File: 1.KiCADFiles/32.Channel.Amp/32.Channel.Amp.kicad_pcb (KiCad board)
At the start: 2 copper layers, 64 x 3 mm, 1 part

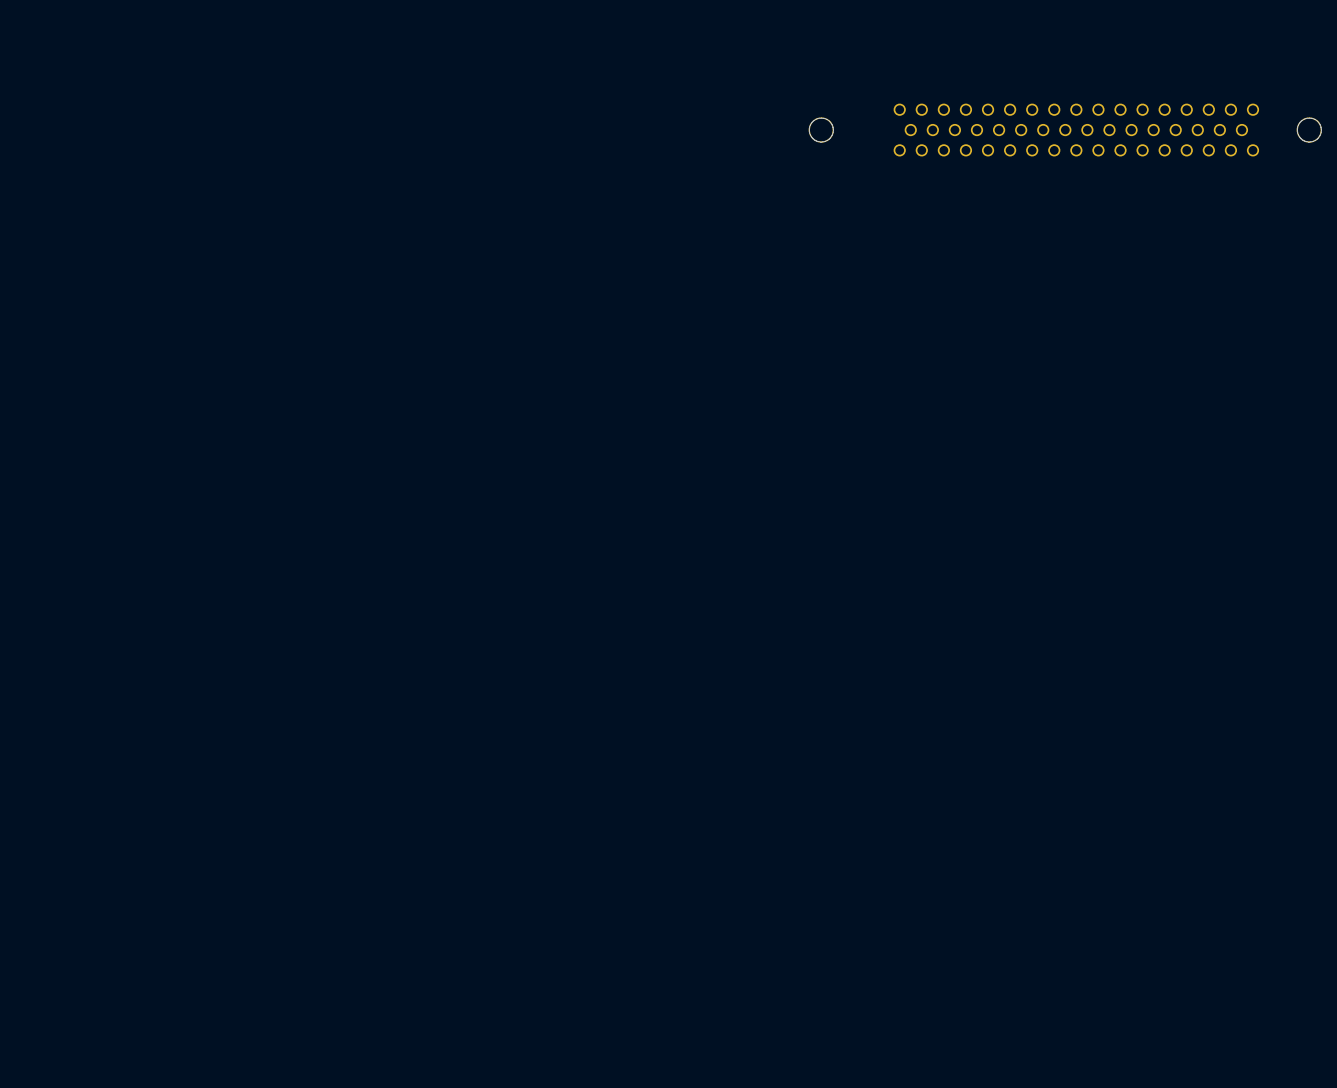
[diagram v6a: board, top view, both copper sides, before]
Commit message: Template Format Created for 32 Channel Amp
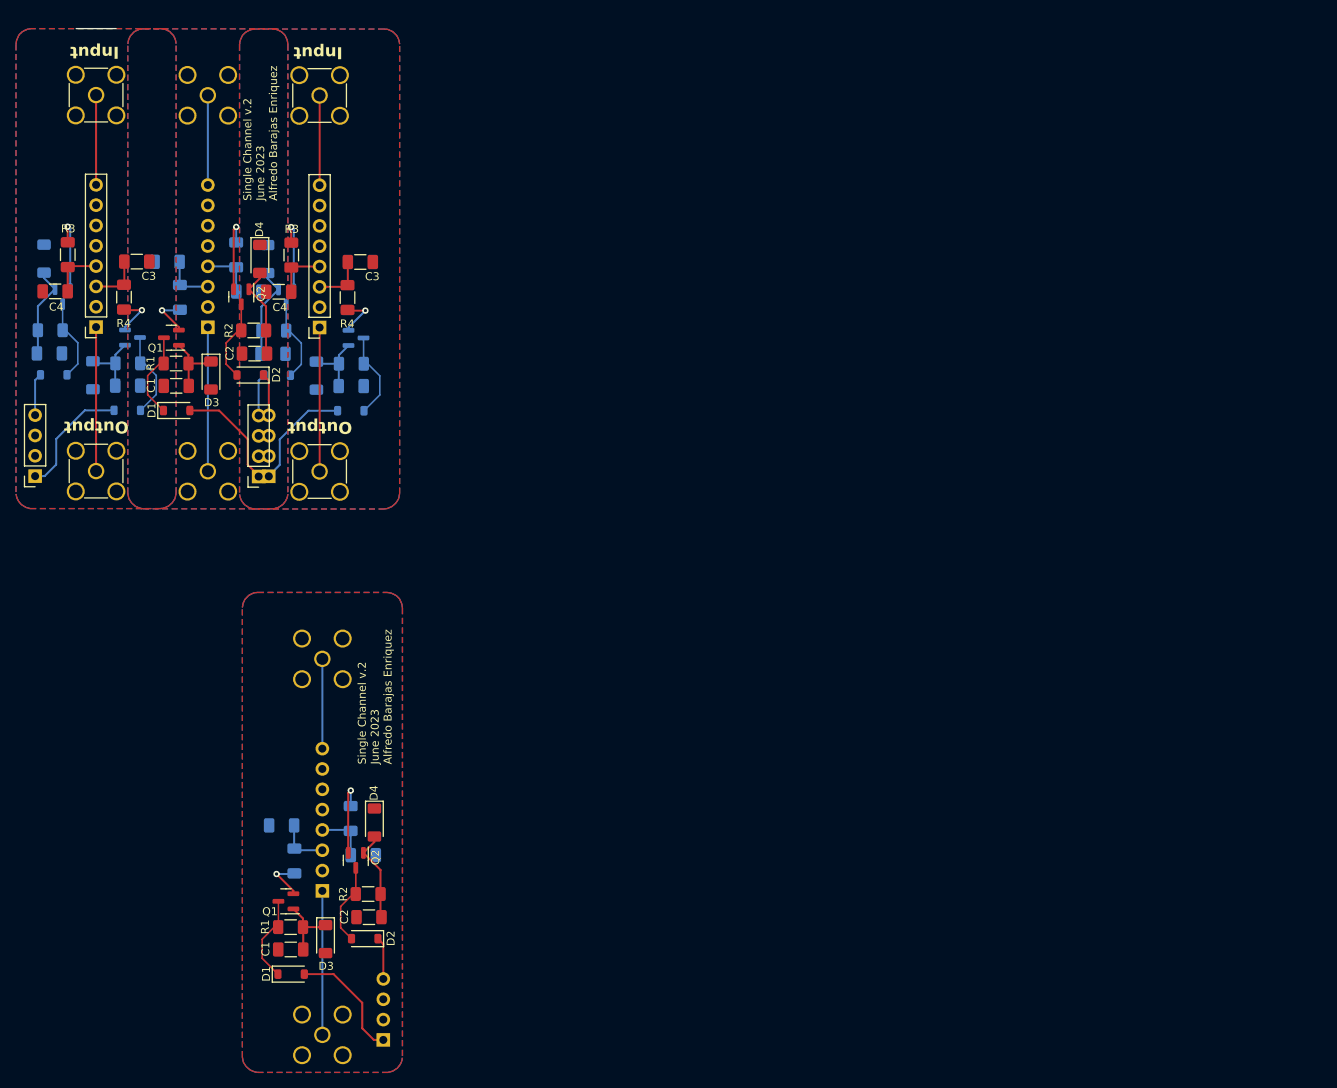
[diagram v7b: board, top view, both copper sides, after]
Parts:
- removed REF**: CONN D-SUB PLUG 50POS RA SLDR, 1.Local.Library:CONN D-SUB PLUG 50POS RA SLDR
- added C1: 10uF, Capacitor_SMD:C_1206_3216Metric_Pad1.33x1.80mm_HandSolder, F.Cu at (31.5, 59.4)
- added C1: 10uF, Capacitor_SMD:C_1206_3216Metric_Pad1.33x1.80mm_HandSolder, F.Cu at (45.8, 129.9)
- added C1: 10uF, Capacitor_SMD:C_1206_3216Metric_Pad1.33x1.80mm_HandSolder, B.Cu at (53.4, 59.5)
- added C1: 10uF, Capacitor_SMD:C_1206_3216Metric_Pad1.33x1.80mm_HandSolder, B.Cu at (25.4, 59.4)
- added C2: 10uF, Capacitor_SMD:C_1206_3216Metric_Pad1.33x1.80mm_HandSolder, F.Cu at (41.3, 55.4)
- added C2: 10uF, Capacitor_SMD:C_1206_3216Metric_Pad1.33x1.80mm_HandSolder, F.Cu at (55.6, 125.9)
- added C2: 10uF, Capacitor_SMD:C_1206_3216Metric_Pad1.33x1.80mm_HandSolder, B.Cu at (15.6, 55.4)
- added C2: 10uF, Capacitor_SMD:C_1206_3216Metric_Pad1.33x1.80mm_HandSolder, B.Cu at (43.6, 55.4)
- added C3: 10uF, Capacitor_SMD:C_1206_3216Metric_Pad1.33x1.80mm_HandSolder, F.Cu at (26.6, 43.9)
- added C3: 10uF, Capacitor_SMD:C_1206_3216Metric_Pad1.33x1.80mm_HandSolder, F.Cu at (54.5, 44.0)
- added C3: 10uF, Capacitor_SMD:C_1206_3216Metric_Pad1.33x1.80mm_HandSolder, B.Cu at (44.7, 114.4)
- added C3: 10uF, Capacitor_SMD:C_1206_3216Metric_Pad1.33x1.80mm_HandSolder, B.Cu at (30.4, 43.9)
- added C4: 10uF, Capacitor_SMD:C_1206_3216Metric_Pad1.33x1.80mm_HandSolder, F.Cu at (44.3, 47.7)
- added C4: 10uF, Capacitor_SMD:C_1206_3216Metric_Pad1.33x1.80mm_HandSolder, F.Cu at (16.4, 47.6)
- added C4: 10uF, Capacitor_SMD:C_1206_3216Metric_Pad1.33x1.80mm_HandSolder, B.Cu at (40.6, 47.7)
- added C4: 10uF, Capacitor_SMD:C_1206_3216Metric_Pad1.33x1.80mm_HandSolder, B.Cu at (54.9, 118.1)
- added D1: 1N4148W, Diode_SMD:D_SOD-123, F.Cu at (45.9, 133.0)
- added D1: 1N4148W, Diode_SMD:D_SOD-123, F.Cu at (31.5, 62.5)
- added D1: 1N4148W, Diode_SMD:D_SOD-123, B.Cu at (25.4, 62.5)
- added D1: 1N4148W, Diode_SMD:D_SOD-123, B.Cu at (53.3, 62.5)
- added D2: 1N4148W, Diode_SMD:D_SOD-123, F.Cu at (40.7, 58.1)
- added D2: 1N4148W, Diode_SMD:D_SOD-123, F.Cu at (55.0, 128.5)
- added D2: 1N4148W, Diode_SMD:D_SOD-123, B.Cu at (44.1, 58.1)
- added D2: 1N4148W, Diode_SMD:D_SOD-123, B.Cu at (16.2, 58.1)
- added D3: BZV55B7V5, Diode_SMD:D_MiniMELF, F.Cu at (50.1, 128.6)
- added D3: BZV55B7V5, Diode_SMD:D_MiniMELF, F.Cu at (35.8, 58.1)
- added D3: BZV55B7V5, Diode_SMD:D_MiniMELF, B.Cu at (49.0, 58.2)
- added D3: BZV55B7V5, Diode_SMD:D_MiniMELF, B.Cu at (21.1, 58.1)
- added D4: BZV55B7V5, Diode_SMD:D_MiniMELF, F.Cu at (56.3, 114.0)
- added D4: BZV55B7V5, Diode_SMD:D_MiniMELF, F.Cu at (41.9, 43.6)
- added D4: BZV55B7V5, Diode_SMD:D_MiniMELF, B.Cu at (15.0, 43.5)
- added D4: BZV55B7V5, Diode_SMD:D_MiniMELF, B.Cu at (42.9, 43.6)
- added J2: Conn_01x08, Connector_PinSocket_2.54mm:PinSocket_1x08_P2.54mm_Vertical, F.Cu at (21.5, 52.1)
- added J2: Conn_01x08, Connector_PinSocket_2.54mm:PinSocket_1x08_P2.54mm_Vertical, F.Cu at (49.4, 52.1)
- added J2: Conn_01x08, Connector_PinSocket_2.54mm:PinSocket_1x08_P2.54mm_Vertical, B.Cu at (35.4, 52.1)
- added J2: Conn_01x08, Connector_PinSocket_2.54mm:PinSocket_1x08_P2.54mm_Vertical, B.Cu at (49.8, 122.6)
- added J3: Conn_01x04, Connector_PinSocket_2.54mm:PinSocket_1x04_P2.54mm_Vertical, F.Cu at (41.8, 70.8)
- added J3: Conn_01x04, Connector_PinSocket_2.54mm:PinSocket_1x04_P2.54mm_Vertical, F.Cu at (13.8, 70.7)
- added J3: Conn_01x04, Connector_PinSocket_2.54mm:PinSocket_1x04_P2.54mm_Vertical, B.Cu at (57.4, 141.2)
- added J3: Conn_01x04, Connector_PinSocket_2.54mm:PinSocket_1x04_P2.54mm_Vertical, B.Cu at (43.1, 70.8)
- added J4: Conn_Coaxial_In, Connector_Coaxial:SMA_Amphenol_901-144_Vertical, F.Cu at (21.5, 23.1)
- added J4: Conn_Coaxial_In, Connector_Coaxial:SMA_Amphenol_901-144_Vertical, F.Cu at (49.4, 23.1)
- added J4: Conn_Coaxial_In, Connector_Coaxial:SMA_Amphenol_901-144_Vertical, B.Cu at (49.8, 93.6)
- added J4: Conn_Coaxial_In, Connector_Coaxial:SMA_Amphenol_901-144_Vertical, B.Cu at (35.4, 23.1)
- added J5: Conn_Coaxial_Out, Connector_Coaxial:SMA_Amphenol_901-144_Vertical, F.Cu at (49.4, 70.1)
- added J5: Conn_Coaxial_Out, Connector_Coaxial:SMA_Amphenol_901-144_Vertical, F.Cu at (21.5, 70.1)
- added J5: Conn_Coaxial_Out, Connector_Coaxial:SMA_Amphenol_901-144_Vertical, B.Cu at (35.4, 70.1)
- added J5: Conn_Coaxial_Out, Connector_Coaxial:SMA_Amphenol_901-144_Vertical, B.Cu at (49.8, 140.6)
- added Q1: MMBT3904, Package_TO_SOT_SMD:SOT-23, F.Cu at (45.2, 123.9)
- added Q1: MMBT3904, Package_TO_SOT_SMD:SOT-23, F.Cu at (30.9, 53.4)
- added Q1: MMBT3904, Package_TO_SOT_SMD:SOT-23, B.Cu at (26.0, 53.4)
- added Q1: MMBT3904, Package_TO_SOT_SMD:SOT-23, B.Cu at (54.0, 53.5)
- added Q2: MMBT3906, Package_TO_SOT_SMD:SOT-23, F.Cu at (53.9, 118.8)
- added Q2: MMBT3906, Package_TO_SOT_SMD:SOT-23, F.Cu at (39.6, 48.3)
- added Q2: MMBT3906, Package_TO_SOT_SMD:SOT-23, B.Cu at (45.2, 48.3)
- added Q2: MMBT3906, Package_TO_SOT_SMD:SOT-23, B.Cu at (17.3, 48.3)
- added R1: 1.0k, Resistor_SMD:R_1206_3216Metric_Pad1.30x1.75mm_HandSolder, F.Cu at (31.5, 56.6)
- added R1: 1.0k, Resistor_SMD:R_1206_3216Metric_Pad1.30x1.75mm_HandSolder, F.Cu at (45.8, 127.1)
- added R1: 1.0k, Resistor_SMD:R_1206_3216Metric_Pad1.30x1.75mm_HandSolder, B.Cu at (53.4, 56.7)
- added R1: 1.0k, Resistor_SMD:R_1206_3216Metric_Pad1.30x1.75mm_HandSolder, B.Cu at (25.4, 56.6)
- added R2: 1.0k, Resistor_SMD:R_1206_3216Metric_Pad1.30x1.75mm_HandSolder, F.Cu at (55.5, 123.0)
- added R2: 1.0k, Resistor_SMD:R_1206_3216Metric_Pad1.30x1.75mm_HandSolder, F.Cu at (41.2, 52.5)
- added R2: 1.0k, Resistor_SMD:R_1206_3216Metric_Pad1.30x1.75mm_HandSolder, B.Cu at (15.7, 52.5)
- added R2: 1.0k, Resistor_SMD:R_1206_3216Metric_Pad1.30x1.75mm_HandSolder, B.Cu at (43.7, 52.5)
- added R3: 4.7, Resistor_SMD:R_1206_3216Metric_Pad1.30x1.75mm_HandSolder, F.Cu at (17.9, 43.0)
- added R3: 4.7, Resistor_SMD:R_1206_3216Metric_Pad1.30x1.75mm_HandSolder, F.Cu at (45.9, 43.1)
- added R3: 4.7, Resistor_SMD:R_1206_3216Metric_Pad1.30x1.75mm_HandSolder, B.Cu at (39.0, 43.1)
- added R3: 4.7, Resistor_SMD:R_1206_3216Metric_Pad1.30x1.75mm_HandSolder, B.Cu at (53.3, 113.5)
- added R4: 4.7, Resistor_SMD:R_1206_3216Metric_Pad1.30x1.75mm_HandSolder, F.Cu at (25.0, 48.4)
- added R4: 4.7, Resistor_SMD:R_1206_3216Metric_Pad1.30x1.75mm_HandSolder, F.Cu at (52.9, 48.4)
- added R4: 4.7, Resistor_SMD:R_1206_3216Metric_Pad1.30x1.75mm_HandSolder, B.Cu at (46.3, 118.8)
- added R4: 4.7, Resistor_SMD:R_1206_3216Metric_Pad1.30x1.75mm_HandSolder, B.Cu at (31.9, 48.4)
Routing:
- net (no net): track 0.00 -> 483.5 mm, vias 0 -> 8
- added copper zone on B.Cu, net (none)
- added copper zone on F.Cu, net (none)
- added copper zone on In1.Cu, net (none)
- added copper zone on In2.Cu, net (none)
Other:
- board outline removed
- copper layers 2 -> 4
- board text added: "Input"
- board text added: "Output"
- board text added: "Single Channel v.2 June 2023 Alfredo Barajas Enriquez"
